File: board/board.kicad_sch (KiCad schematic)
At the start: 3 parts, among them J1 001_I2C, J2 001_I2C

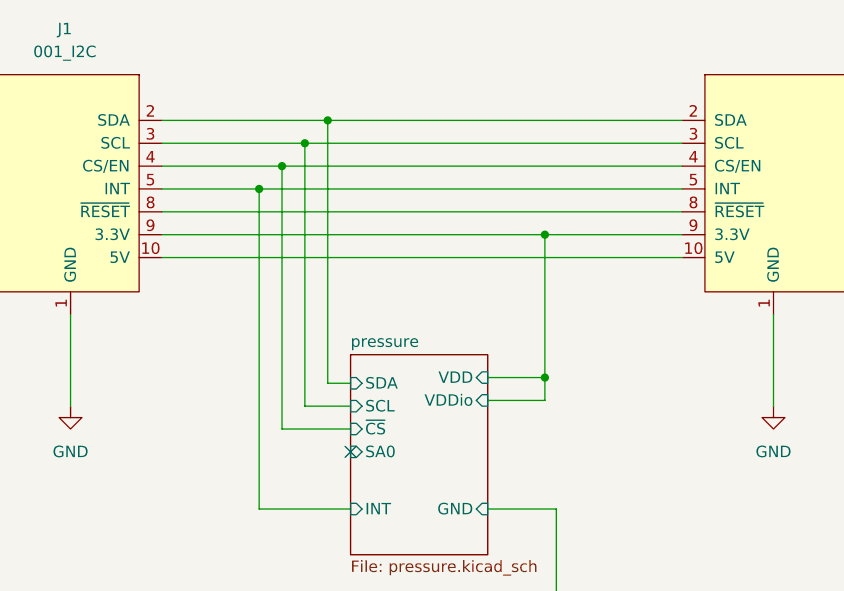
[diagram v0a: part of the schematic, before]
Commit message: added ground plane
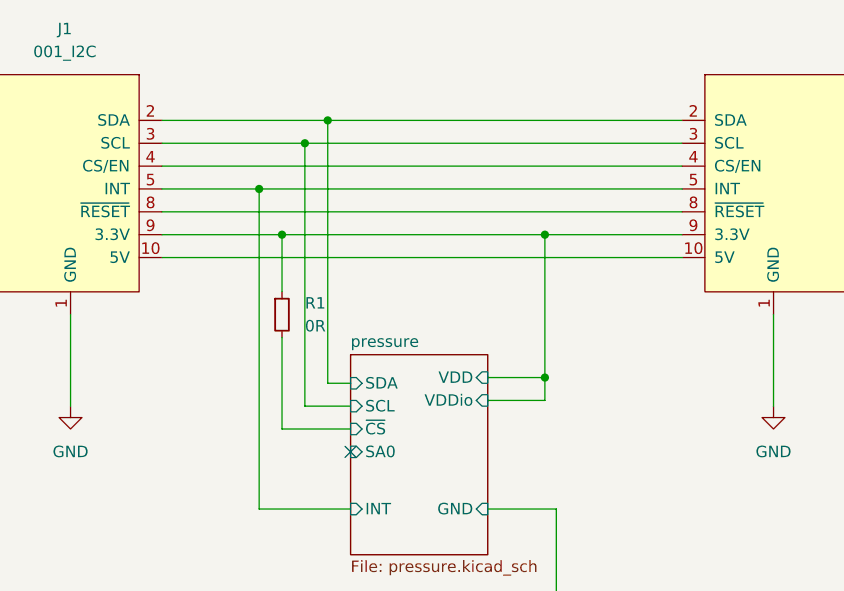
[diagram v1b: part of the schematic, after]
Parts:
- added R1: 0R, Resistor_SMD:R_0603_1608Metric, symbol Device:R_Small
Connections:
- net pressure/VDD: now also R1.1
- net pressure/~{CS}: now also R1.2; no longer J1.4 (CS/EN), J2.4 (CS/EN)
- new net: J1.4 (CS/EN), J2.4 (CS/EN)
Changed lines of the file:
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@@
   (junction (at 149.86 79.375) (diameter 0) (color 0 0 0 0)
   )
-  (junction (at 120.65 71.755) (diameter 0) (color 0 0 0 0)
-  )
   (junction (at 125.73 66.675) (diameter 0) (color 0 0 0 0)
   )
+  (junction (at 120.65 79.375) (diameter 0) (color 0 0 0 0)
+  )
   (junction (at 118.11 74.295) (diameter 0) (color 0 0 0 0)
   )
   (no_connect (at 128.27 103.505))
+  (wire (pts (xy 120.65 79.375) (xy 149.86 79.375))
+    (stroke (width 0) (type default) (color 0 0 0 0))
+  )
   (wire (pts (xy 149.86 95.25) (xy 149.86 79.375))
     (stroke (width 0) (type default) (color 0 0 0 0))
@@
     (stroke (width 0) (type default) (color 0 0 0 0))
   )
-  (wire (pts (xy 107.315 79.375) (xy 149.86 79.375))
+  (wire (pts (xy 107.315 79.375) (xy 120.65 79.375))
     (stroke (width 0) (type default) (color 0 0 0 0))
   )
@@
     (stroke (width 0) (type default) (color 0 0 0 0))
   )
-  (wire (pts (xy 120.65 100.965) (xy 120.65 71.755))
+  (wire (pts (xy 120.65 100.965) (xy 120.65 90.805))
     (stroke (width 0) (type default) (color 0 0 0 0))
   )
@@
     (stroke (width 0) (type default) (color 0 0 0 0))
   )
-  (wire (pts (xy 120.65 71.755) (xy 165.1 71.755))
-    (stroke (width 0) (type default) (color 0 0 0 0))
-  )
   (wire (pts (xy 97.155 88.265) (xy 97.155 98.425))
     (stroke (width 0) (type default) (color 0 0 0 0))
@@
     (stroke (width 0) (type default) (color 0 0 0 0))
   )
-  (wire (pts (xy 107.315 71.755) (xy 120.65 71.755))
+  (wire (pts (xy 107.315 71.755) (xy 165.1 71.755))
+    (stroke (width 0) (type default) (color 0 0 0 0))
+  )
+  (wire (pts (xy 120.65 79.375) (xy 120.65 85.725))
     (stroke (width 0) (type default) (color 0 0 0 0))
   )
@@
     (pin "9")
   )
+  (symbol (lib_id "Device:R_Small") (at 120.65 88.265 0) (unit 1)
+    (in_bom yes) (on_board yes) (fields_autoplaced)
+    (property "Reference" "R1" (id 0) (at 123.19 86.9949 0)
+      (effects (font (size 1.27 1.27)) (justify left))
+    )
+    (property "Value" "0R" (id 1) (at 123.19 89.5349 0)
+      (effects (font (size 1.27 1.27)) (justify left))
+    )
+    (property "Footprint" "Resistor_SMD:R_0603_1608Metric" (id 2) (at 120.65 88.265 0)
+      (effects (font (size 1.27 1.27)) hide)
+    )
+    (property "Datasheet" "~" (id 3) (at 120.65 88.265 0)
+      (effects (font (size 1.27 1.27)) hide)
+    )
+    (pin "1")
+    (pin "2")
+  )
   (symbol (lib_id "power:GND") (at 175.26 98.425 0) (unit 1)
     (in_bom yes) (on_board yes) (fields_autoplaced)
@@
       (reference "LOGO1") (unit 1) (value "Logo_Open_Hardware_Small") (footprint "Symbol:OSHW-Symbol_6.7x6mm_SilkScreen")
     )
+    (path "/3e02d05d-f3b8-4d09-8dd0-d33718d24255"
+      (reference "R1") (unit 1) (value "0R") (footprint "Resistor_SMD:R_0603_1608Metric")
+    )
     (path "/767ce4c6-0e55-4543-92f0-34cb8237a544/06981c94-72ea-43b4-a7ca-80959a1a7f83"
